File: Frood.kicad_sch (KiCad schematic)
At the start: 42 parts, among them J1 Left, J2 Right, J3 Bottom, SW1 RESET, SW2 BOOT, U1 RP2040, U2 W25Q32JWUUIQ, U3 TLV73333PDBVR, Y1 X322512MSB4SI

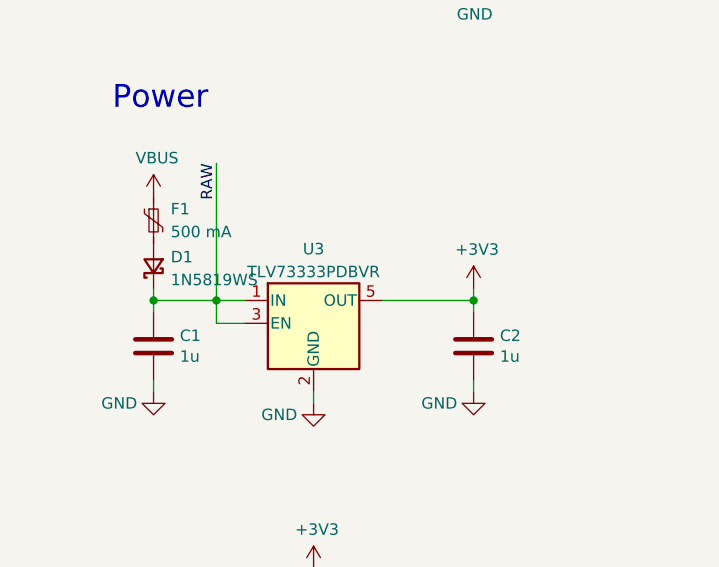
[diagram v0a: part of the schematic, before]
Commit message: Rename to Frood; use a 500 mA regulator; update README
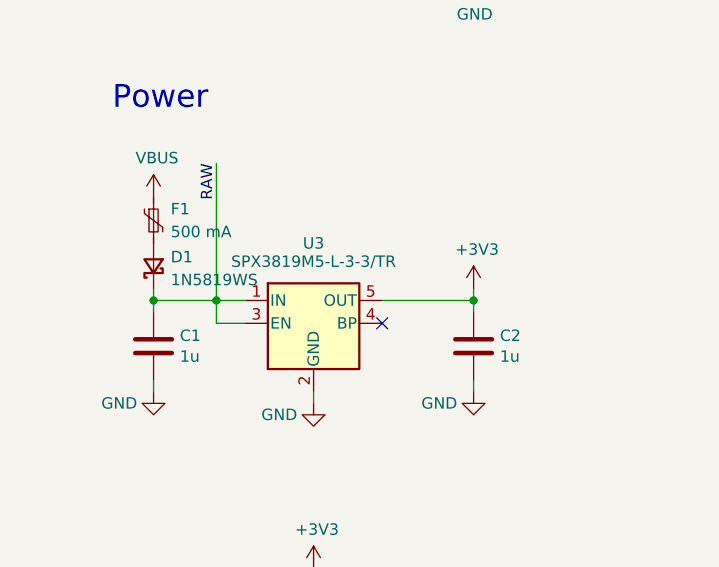
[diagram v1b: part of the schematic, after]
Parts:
- U3: value TLV73333PDBVR -> SPX3819M5-L-3-3/TR; symbol Regulator_Linear:TLV73333PDBV -> Regulator_Linear:SPX3819M5-L-3-3
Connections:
- no-connect marks 10 -> 11
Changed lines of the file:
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@@
   (no_connect (at 139.7 136.525))
   (no_connect (at 203.2 132.715))
+  (no_connect (at 53.975 111.125))
   (no_connect (at 203.2 135.255))
   (no_connect (at 37.465 43.815))
@@
     )
   )
-  (symbol (lib_id "Regulator_Linear:TLV73333PDBV") (at 46.355 111.125 0) (unit 1)
-    (in_bom yes) (on_board yes) (fields_autoplaced)
-    (property "Reference" "U3" (id 0) (at 46.355 102.87 0))
-    (property "Value" "TLV73333PDBVR" (id 1) (at 46.355 105.41 0))
+  (symbol (lib_id "Regulator_Linear:SPX3819M5-L-3-3") (at 46.355 111.125 0) (unit 1)
+    (in_bom yes) (on_board yes)
+    (property "Reference" "U3" (id 0) (at 46.355 102.235 0))
+    (property "Value" "SPX3819M5-L-3-3/TR" (id 1) (at 46.355 104.267 0))
     (property "Footprint" "Package_TO_SOT_SMD:SOT-23-5" (id 2) (at 46.355 102.87 0)
-      (effects (font (size 1.27 1.27) italic) hide)
-    )
-    (property "Datasheet" "http://www.ti.com/lit/ds/symlink/tlv733p.pdf" (id 3) (at 46.355 111.125 0)
+      (effects (font (size 1.27 1.27)) hide)
+    )
+    (property "Datasheet" "https://www.exar.com/content/document.ashx?id=22106&languageid=1033&type=Datasheet&partnumber=SPX3819&filename=SPX3819.pdf&part=SPX3819" (id 3) (at 46.355 111.125 0)
       (effects (font (size 1.27 1.27)) hide)
     )
@@
     )
     (path "/c779cfe3-909f-43ee-bfb4-4bb9da9ab75d"
-      (reference "U3") (unit 1) (value "TLV73333PDBVR") (footprint "Package_TO_SOT_SMD:SOT-23-5")
+      (reference "U3") (unit 1) (value "SPX3819M5-L-3-3/TR") (footprint "Package_TO_SOT_SMD:SOT-23-5")
     )
     (path "/22bd63ac-0dc8-46a4-b634-819479c04be4"

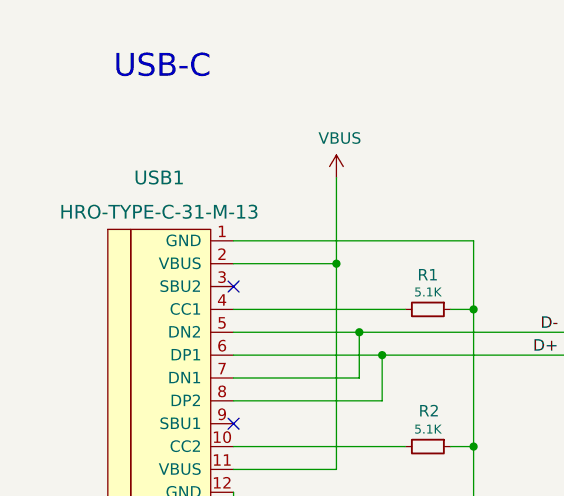
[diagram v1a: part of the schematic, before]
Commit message: Fix the USB-C socket value; Use an in-stock 27R resistor
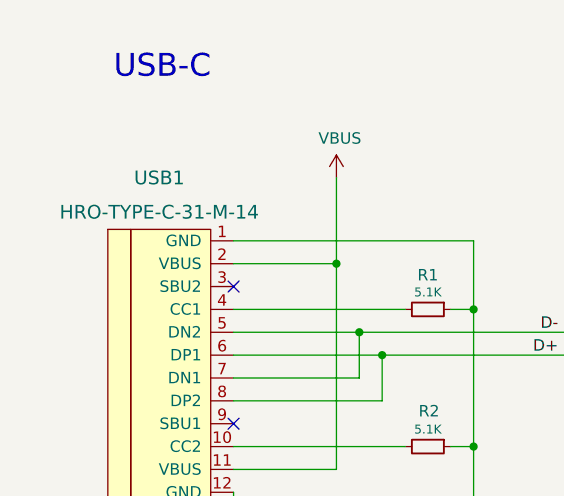
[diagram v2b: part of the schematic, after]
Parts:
- USB1: value HRO-TYPE-C-31-M-13 -> HRO-TYPE-C-31-M-14
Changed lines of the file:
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@@
       (effects (font (size 1.524 1.524)))
     )
-    (property "Value" "HRO-TYPE-C-31-M-13" (id 1) (at 29.21 35.56 0)
+    (property "Value" "HRO-TYPE-C-31-M-14" (id 1) (at 29.21 35.56 0)
       (effects (font (size 1.524 1.524)))
     )
@@
     )
     (path "/22bd63ac-0dc8-46a4-b634-819479c04be4"
-      (reference "USB1") (unit 1) (value "HRO-TYPE-C-31-M-13") (footprint "42keebs:TYPE-C-31-M-14-PiMicro")
+      (reference "USB1") (unit 1) (value "HRO-TYPE-C-31-M-14") (footprint "42keebs:TYPE-C-31-M-14-PiMicro")
     )
     (path "/dec5c5bc-8eeb-4827-91ed-4f4f63dc849a"

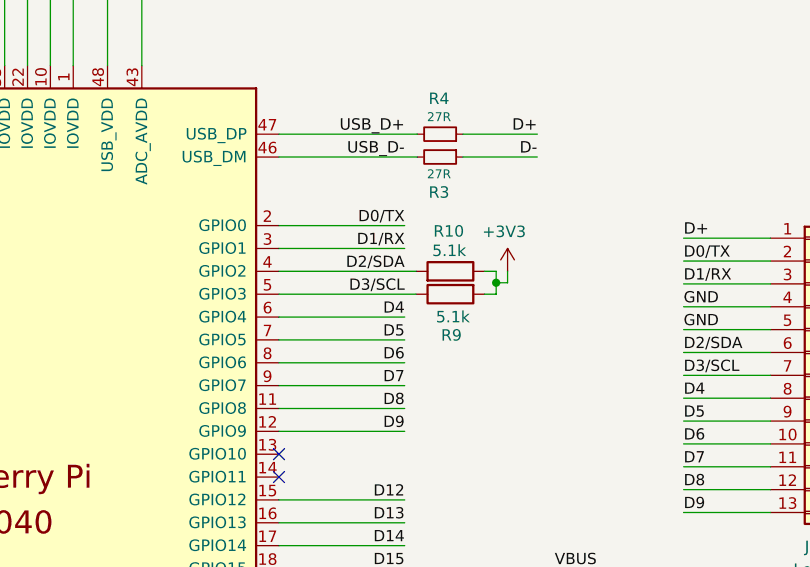
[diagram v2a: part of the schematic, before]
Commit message: Drop the forced I2C pull-up resistors; Add flash 3D model
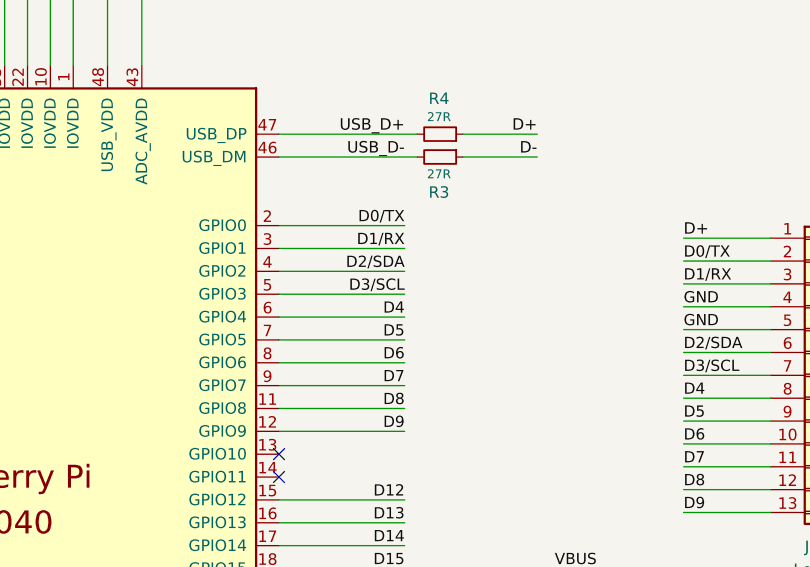
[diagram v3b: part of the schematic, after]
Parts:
- removed R10, R9: 5.1k, Resistor_SMD:R_0402_1005Metric, symbol Device:R
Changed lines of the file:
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@@
   (junction (at 153.67 41.275) (diameter 0) (color 0 0 0 0)
-  )
-  (junction (at 227.33 78.105) (diameter 0) (color 0 0 0 0)
   )
   (junction (at 229.108 120.015) (diameter 0) (color 0 0 0 0)
@@
     (stroke (width 0) (type default) (color 0 0 0 0))
   )
-  (wire (pts (xy 228.6 76.835) (xy 228.6 78.105))
-    (stroke (width 0) (type default) (color 0 0 0 0))
-  )
   (wire (pts (xy 191.135 198.12) (xy 201.295 198.12))
     (stroke (width 0) (type default) (color 0 0 0 0))
@@
     (stroke (width 0) (type default) (color 0 0 0 0))
   )
-  (wire (pts (xy 228.6 78.105) (xy 227.33 78.105))
-    (stroke (width 0) (type default) (color 0 0 0 0))
-  )
   (wire (pts (xy 28.575 117.475) (xy 28.575 118.745))
     (stroke (width 0) (type default) (color 0 0 0 0))
@@
     (stroke (width 0) (type default) (color 0 0 0 0))
   )
-  (wire (pts (xy 227.33 79.375) (xy 226.06 79.375))
-    (stroke (width 0) (type default) (color 0 0 0 0))
-  )
   (wire (pts (xy 272.542 132.842) (xy 272.542 123.19))
     (stroke (width 0) (type default) (color 0 0 0 0))
@@
     (stroke (width 0) (type default) (color 0 0 0 0))
   )
-  (wire (pts (xy 227.33 78.105) (xy 227.33 79.375))
-    (stroke (width 0) (type default) (color 0 0 0 0))
-  )
   (wire (pts (xy 217.297 20.955) (xy 228.727 20.955))
     (stroke (width 0) (type default) (color 0 0 0 0))
@@
     (stroke (width 0) (type default) (color 0 0 0 0))
   )
-  (wire (pts (xy 203.2 76.835) (xy 218.44 76.835))
-    (stroke (width 0) (type default) (color 0 0 0 0))
-  )
   (wire (pts (xy 248.158 83.312) (xy 257.81 83.312))
     (stroke (width 0) (type default) (color 0 0 0 0))
@@
     (stroke (width 0) (type default) (color 0 0 0 0))
   )
-  (wire (pts (xy 226.06 76.835) (xy 227.33 76.835))
-    (stroke (width 0) (type default) (color 0 0 0 0))
-  )
   (wire (pts (xy 280.67 73.152) (xy 290.322 73.152))
     (stroke (width 0) (type default) (color 0 0 0 0))
@@
     (stroke (width 0) (type default) (color 0 0 0 0))
   )
-  (wire (pts (xy 227.33 76.835) (xy 227.33 78.105))
-    (stroke (width 0) (type default) (color 0 0 0 0))
-  )
   (wire (pts (xy 280.67 88.392) (xy 290.322 88.392))
     (stroke (width 0) (type default) (color 0 0 0 0))
@@
     (stroke (width 0) (type default) (color 0 0 0 0))
   )
+  (wire (pts (xy 203.2 76.835) (xy 217.17 76.835))
+    (stroke (width 0) (type default) (color 0 0 0 0))
+  )
   (wire (pts (xy 248.158 78.232) (xy 257.81 78.232))
     (stroke (width 0) (type default) (color 0 0 0 0))
@@
     (stroke (width 0) (type default) (color 0 0 0 0))
   )
-  (wire (pts (xy 203.2 79.375) (xy 218.44 79.375))
-    (stroke (width 0) (type default) (color 0 0 0 0))
-  )
   (wire (pts (xy 217.17 130.175) (xy 203.2 130.175))
     (stroke (width 0) (type default) (color 0 0 0 0))
@@
   )
   (wire (pts (xy 150.495 187.96) (xy 147.955 187.96))
+    (stroke (width 0) (type default) (color 0 0 0 0))
+  )
+  (wire (pts (xy 203.2 79.375) (xy 217.17 79.375))
     (stroke (width 0) (type default) (color 0 0 0 0))
   )
@@
     )
     (pin "1")
-  )
-  (symbol (lib_id "Device:R") (at 222.25 76.835 270) (mirror x) (unit 1)
-    (in_bom yes) (on_board yes)
-    (property "Reference" "R10" (id 0) (at 220.345 72.39 90)
-      (effects (font (size 1.27 1.27)) (justify left))
-    )
-    (property "Value" "5.1k" (id 1) (at 220.218 74.549 90)
-      (effects (font (size 1.27 1.27)) (justify left))
-    )
-    (property "Footprint" "Resistor_SMD:R_0402_1005Metric" (id 2) (at 222.25 78.613 90)
-      (effects (font (size 1.27 1.27)) hide)
-    )
-    (property "Datasheet" "~" (id 3) (at 222.25 76.835 0)
-      (effects (font (size 1.27 1.27)) hide)
-    )
-    (pin "1")
-    (pin "2")
   )
   (symbol (lib_id "power:+3V3") (at 169.926 227.076 0) (unit 1)
@@
     (pin "2")
   )
-  (symbol (lib_id "Device:R") (at 222.25 79.375 90) (mirror x) (unit 1)
-    (in_bom yes) (on_board yes)
-    (property "Reference" "R9" (id 0) (at 223.52 83.947 90)
-      (effects (font (size 1.27 1.27)) (justify left))
-    )
-    (property "Value" "5.1k" (id 1) (at 224.409 81.915 90)
-      (effects (font (size 1.27 1.27)) (justify left))
-    )
-    (property "Footprint" "Resistor_SMD:R_0402_1005Metric" (id 2) (at 222.25 77.597 90)
-      (effects (font (size 1.27 1.27)) hide)
-    )
-    (property "Datasheet" "~" (id 3) (at 222.25 79.375 0)
-      (effects (font (size 1.27 1.27)) hide)
-    )
-    (pin "1")
-    (pin "2")
-  )
   (symbol (lib_id "Type-C:HRO-TYPE-C-31-M-12") (at 34.925 52.705 0) (unit 1)
     (in_bom yes) (on_board yes) (fields_autoplaced)
@@
     (pin "1")
     (pin "2")
-  )
-  (symbol (lib_id "power:+3V3") (at 228.6 76.835 0) (mirror y) (unit 1)
-    (in_bom yes) (on_board yes)
-    (property "Reference" "#PWR04" (id 0) (at 228.6 80.645 0)
-      (effects (font (size 1.27 1.27)) hide)
-    )
-    (property "Value" "+3V3" (id 1) (at 228.219 72.4408 0))
-    (property "Footprint" "" (id 2) (at 228.6 76.835 0)
-      (effects (font (size 1.27 1.27)) hide)
-    )
-    (property "Datasheet" "" (id 3) (at 228.6 76.835 0)
-      (effects (font (size 1.27 1.27)) hide)
-    )
-    (pin "1")
   )
   (symbol (lib_id "Device:R") (at 139.446 252.476 270) (unit 1)
@@
       (reference "#PWR03") (unit 1) (value "GND") (footprint "")
     )
-    (path "/35d84a2a-9182-4f52-b52c-368846f7ca3d"
-      (reference "#PWR04") (unit 1) (value "+3V3") (footprint "")
-    )
     (path "/3f2af67c-5973-4490-abf7-23239e2b72e1"
       (reference "#PWR05") (unit 1) (value "GND") (footprint "")
@@
       (reference "R8") (unit 1) (value "10k") (footprint "Resistor_SMD:R_0402_1005Metric")
     )
-    (path "/1cec9fb3-3d3e-4909-8a8b-6b132daa8fc6"
-      (reference "R9") (unit 1) (value "5.1k") (footprint "Resistor_SMD:R_0402_1005Metric")
-    )
-    (path "/04fbb4a5-6e76-42bf-809d-79ff02086d54"
-      (reference "R10") (unit 1) (value "5.1k") (footprint "Resistor_SMD:R_0402_1005Metric")
-    )
     (path "/d7117139-be7b-46b7-965e-4e771ccb0de3"
